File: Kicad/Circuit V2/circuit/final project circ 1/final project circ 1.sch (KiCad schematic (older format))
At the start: 87 parts, among them J1 USB_B_Micro, J10 Conn_01x02_Female, J11 Conn_01x02_Female, J12 Conn_01x02_Female, J2 Conn_01x01_Female, J3 Conn_01x04_Female, J4 Conn_01x04_Female, J5 Conn_01x03_Female, J6 Conn_01x03_Female, J7 Conn_01x04_Female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

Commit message: "finalized" the grounding stuff fixed more connections. Relay and Screw terminal still needs to be done. I should be able to finish it tonight
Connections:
- net +VDC: now also C12.1; no longer C12.2, U7.2 (Vin)
- net 12v: now also C10.1, C8.1, C9.1; no longer C10.2, C8.2, C9.2
- net GND1: now also C10.2, C11.2, C12.2, C13.2, C8.2, C9.2; no longer C10.1, C11.1, C12.1, C13.1, C8.1, C9.1
- net LINE: now also U7.2 (Vin)
- net at D3.1 (K), D4.1 (K), Q6.3 (C)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: now also C11.1; no longer C11.2
- net at D5.1 (K), Q6.1 (B), R8.1: now also C13.1; no longer C13.2
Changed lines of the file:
@@
 EESchema Schematic File Version 4
-EELAYER 30 0
+LIBS:final project circ 1-cache
+EELAYER 29 0
 EELAYER END
 $Descr A0 46811 33110
@@
 F 3 "~" H 18550 16550 50  0001 C CNN
 	1    18550 16550
-	-1   0    0    1
+	1    0    0    -1
 $EndComp
 $Comp
@@
 F 3 "~" H 19000 16550 50  0001 C CNN
 	1    19000 16550
-	-1   0    0    1
+	1    0    0    -1
 $EndComp
 Wire Wire Line
@@
 F 3 "~" H 19450 16550 50  0001 C CNN
 	1    19450 16550
-	-1   0    0    1
+	1    0    0    -1
 $EndComp
 Wire Wire Line
@@
 F 3 "~" H 15550 13800 50  0001 C CNN
 	1    15550 13800
-	-1   0    0    1
+	1    0    0    -1
 $EndComp
 Wire Wire Line
@@
 F 3 "~" H 16900 13900 50  0001 C CNN
 	1    16900 13900
-	-1   0    0    1
+	1    0    0    -1
 $EndComp
 Wire Wire Line
@@
 F 3 "~" H 16300 14450 50  0001 C CNN
 	1    16300 14450
-	-1   0    0    1
+	1    0    0    -1
 $EndComp
 Wire Wire Line
@@
 	1    0    0    -1
 $EndComp
-$Comp
-L power:+VDC #PWR036
-U 1 1 62176DF4
-P 19350 17950
-F 0 "#PWR036" H 19350 17850 50  0001 C CNN
-F 1 "+VDC" H 19350 18225 50  0000 C CNN
-F 2 "" H 19350 17950 50  0001 C CNN
-F 3 "" H 19350 17950 50  0001 C CNN
-	1    19350 17950
-	0    -1   -1   0
-$EndComp
-Wire Wire Line
-	19350 17950 19500 17950
 Wire Wire Line
 	19500 17950 19500 18000
@@
 Wire Wire Line
 	25700 10850 25700 10900
+$Comp
+L power:LINE #PWR0126
+U 1 1 6218464F
+P 19350 17950
+F 0 "#PWR0126" H 19350 17800 50  0001 C CNN
+F 1 "LINE" H 19367 18123 50  0000 C CNN
+F 2 "" H 19350 17950 50  0001 C CNN
+F 3 "" H 19350 17950 50  0001 C CNN
+	1    19350 17950
+	1    0    0    -1
+$EndComp
+Wire Wire Line
+	19350 17950 19500 17950
 $EndSCHEMATC

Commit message: one trace left baby!!
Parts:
- added C24: 100p, Capacitor_SMD:C_1210_3225Metric, symbol Device:C
- added OJ1, OJ2, OJ3, OJ4, OJ5, OJ6: SolderJumper_2_Open, Jumper:SolderJumper-2_P1.3mm_Open_Pad1.0x1.5mm, symbol Jumper:SolderJumper_2_Open
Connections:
- net GND: now also C24.1, OJ1.2 (B), OJ2.2 (B), OJ3.2 (B), OJ4.2 (B), OJ5.2 (B), OJ6.2 (B)
- net GND1: now also C24.2, OJ1.1 (A), OJ2.1 (A), OJ3.1 (A), OJ4.1 (A), OJ5.1 (A), OJ6.1 (A)
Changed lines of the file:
@@
 Wire Wire Line
 	19350 17950 19500 17950
+$Comp
+L final-project-circ-1-rescue:GND1-power #PWR?
+U 1 1 621A9CC9
+P 19300 21100
+F 0 "#PWR?" H 19300 20850 50  0001 C CNN
+F 1 "GND1" V 19305 20972 50  0000 R CNN
+F 2 "" H 19300 21100 50  0001 C CNN
+F 3 "" H 19300 21100 50  0001 C CNN
+	1    19300 21100
+	1    0    0    -1
+$EndComp
+$Comp
+L power:GND #PWR?
+U 1 1 621AB680
+P 19700 21100
+F 0 "#PWR?" H 19700 20850 50  0001 C CNN
+F 1 "GND" H 19705 20927 50  0000 C CNN
+F 2 "" H 19700 21100 50  0001 C CNN
+F 3 "" H 19700 21100 50  0001 C CNN
+	1    19700 21100
+	1    0    0    -1
+$EndComp
+$Comp
+L Device:C C24
+U 1 1 621ABDF7
+P 19500 21000
+F 0 "C24" V 19650 21000 50  0000 C CNN
+F 1 "100p" V 19339 21000 50  0000 C CNN
+F 2 "Capacitor_SMD:C_1210_3225Metric" H 19538 20850 50  0001 C CNN
+F 3 "~" H 19500 21000 50  0001 C CNN
+	1    19500 21000
+	0    1    1    0
+$EndComp
+Wire Wire Line
+	19350 21000 19300 21000
+Wire Wire Line
+	19300 21000 19300 21100
+Wire Wire Line
+	19650 21000 19700 21000
+Wire Wire Line
+	19700 21000 19700 21100
+$Comp
+L Jumper:SolderJumper_2_Open OJ1
+U 1 1 621F7E25
+P 19500 19200
+F 0 "OJ1" H 19500 19405 50  0000 C CNN
+F 1 "SolderJumper_2_Open" H 19500 19314 50  0000 C CNN
+F 2 "Jumper:SolderJumper-2_P1.3mm_Open_Pad1.0x1.5mm" H 19500 19200 50  0001 C CNN
+F 3 "~" H 19500 19200 50  0001 C CNN
+	1    19500 19200
+	1    0    0    -1
+$EndComp
+$Comp
+L Jumper:SolderJumper_2_Open OJ2
+U 1 1 62220007
+P 19500 19500
+F 0 "OJ2" H 19500 19705 50  0000 C CNN
+F 1 "SolderJumper_2_Open" H 19500 19614 50  0000 C CNN
+F 2 "Jumper:SolderJumper-2_P1.3mm_Open_Pad1.0x1.5mm" H 19500 19500 50  0001 C CNN
+F 3 "~" H 19500 19500 50  0001 C CNN
+	1    19500 19500
+	1    0    0    -1
+$EndComp
+$Comp
+L Jumper:SolderJumper_2_Open OJ3
+U 1 1 6222057A
+P 19500 19800
+F 0 "OJ3" H 19500 20005 50  0000 C CNN
+F 1 "SolderJumper_2_Open" H 19500 19914 50  0000 C CNN
+F 2 "Jumper:SolderJumper-2_P1.3mm_Open_Pad1.0x1.5mm" H 19500 19800 50  0001 C CNN
+F 3 "~" H 19500 19800 50  0001 C CNN
+	1    19500 19800
+	1    0    0    -1
+$EndComp
+$Comp
+L Jumper:SolderJumper_2_Open OJ4
+U 1 1 622208CB
+P 19500 20100
+F 0 "OJ4" H 19500 20305 50  0000 C CNN
+F 1 "SolderJumper_2_Open" H 19500 20214 50  0000 C CNN
+F 2 "Jumper:SolderJumper-2_P1.3mm_Open_Pad1.0x1.5mm" H 19500 20100 50  0001 C CNN
+F 3 "~" H 19500 20100 50  0001 C CNN
+	1    19500 20100
+	1    0    0    -1
+$EndComp
+$Comp
+L Jumper:SolderJumper_2_Open OJ5
+U 1 1 62247E3F
+P 19500 20400
+F 0 "OJ5" H 19500 20605 50  0000 C CNN
+F 1 "SolderJumper_2_Open" H 19500 20514 50  0000 C CNN
+F 2 "Jumper:SolderJumper-2_P1.3mm_Open_Pad1.0x1.5mm" H 19500 20400 50  0001 C CNN
+F 3 "~" H 19500 20400 50  0001 C CNN
+	1    19500 20400
+	1    0    0    -1
+$EndComp
+$Comp
+L Jumper:SolderJumper_2_Open OJ6
+U 1 1 622482E1
+P 19500 20700
+F 0 "OJ6" H 19500 20905 50  0000 C CNN
+F 1 "SolderJumper_2_Open" H 19500 20814 50  0000 C CNN
+F 2 "Jumper:SolderJumper-2_P1.3mm_Open_Pad1.0x1.5mm" H 19500 20700 50  0001 C CNN
+F 3 "~" H 19500 20700 50  0001 C CNN
+	1    19500 20700
+	1    0    0    -1
+$EndComp
+Wire Wire Line
+	19350 19200 19300 19200
+Wire Wire Line
+	19300 19200 19300 19500
+Connection ~ 19300 21000
+Wire Wire Line
+	19650 19200 19700 19200
+Wire Wire Line
+	19700 19200 19700 19500
+Connection ~ 19700 21000
+Wire Wire Line
+	19650 19500 19700 19500
+Connection ~ 19700 19500
+Wire Wire Line
+	19700 19500 19700 19800
+Wire Wire Line
+	19350 19500 19300 19500
+Connection ~ 19300 19500
+Wire Wire Line
+	19300 19500 19300 19800
+Wire Wire Line
+	19650 19800 19700 19800
+Connection ~ 19700 19800
+Wire Wire Line
+	19700 19800 19700 20100
+Wire Wire Line
+	19350 19800 19300 19800
+Connection ~ 19300 19800
+Wire Wire Line
+	19300 19800 19300 20100
+Wire Wire Line
+	19350 20100 19300 20100
+Connection ~ 19300 20100
+Wire Wire Line
+	19300 20100 19300 20400
+Wire Wire Line
+	19650 20100 19700 20100
+Connection ~ 19700 20100
+Wire Wire Line
+	19700 20100 19700 20400
+Wire Wire Line
+	19650 20400 19700 20400
+Connection ~ 19700 20400
+Wire Wire Line
+	19700 20400 19700 20700
+Wire Wire Line
+	19350 20400 19300 20400
+Connection ~ 19300 20400
+Wire Wire Line
+	19300 20400 19300 20700
+Wire Wire Line
+	19350 20700 19300 20700
+Connection ~ 19300 20700
+Wire Wire Line
+	19300 20700 19300 21000
+Wire Wire Line
+	19650 20700 19700 20700
+Connection ~ 19700 20700
+Wire Wire Line
+	19700 20700 19700 21000
 $EndSCHEMATC

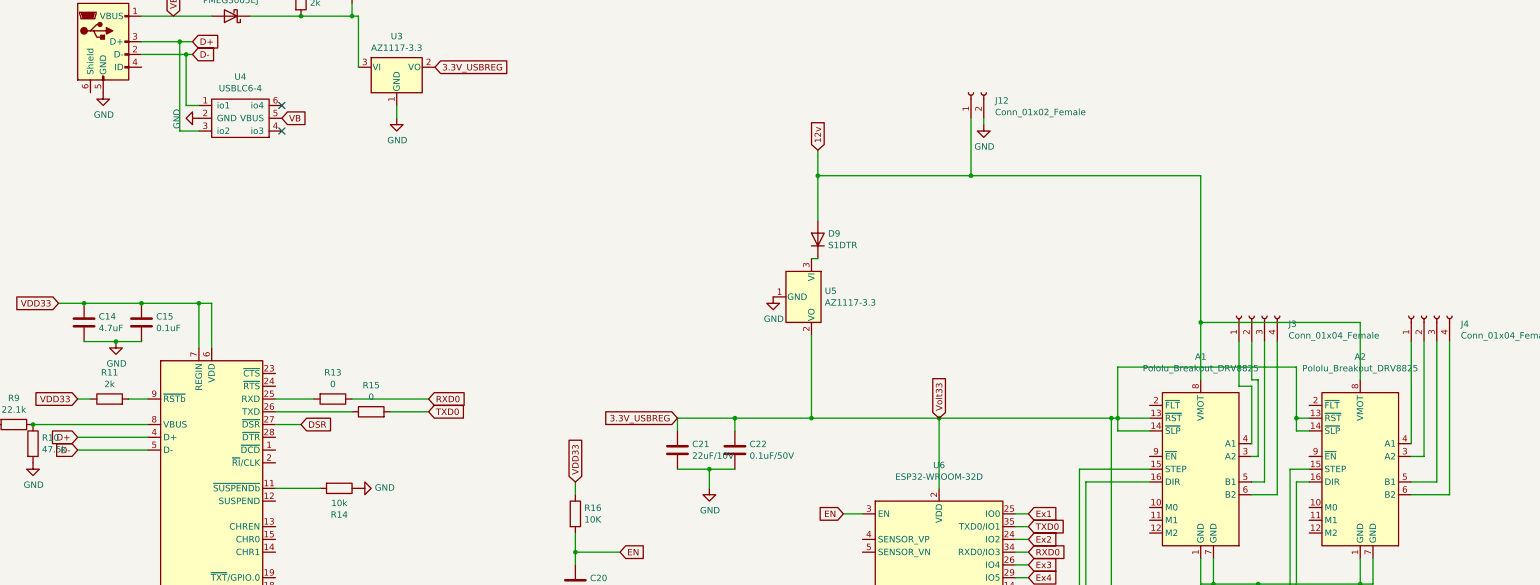
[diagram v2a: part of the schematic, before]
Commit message: changed stepper driver pinout
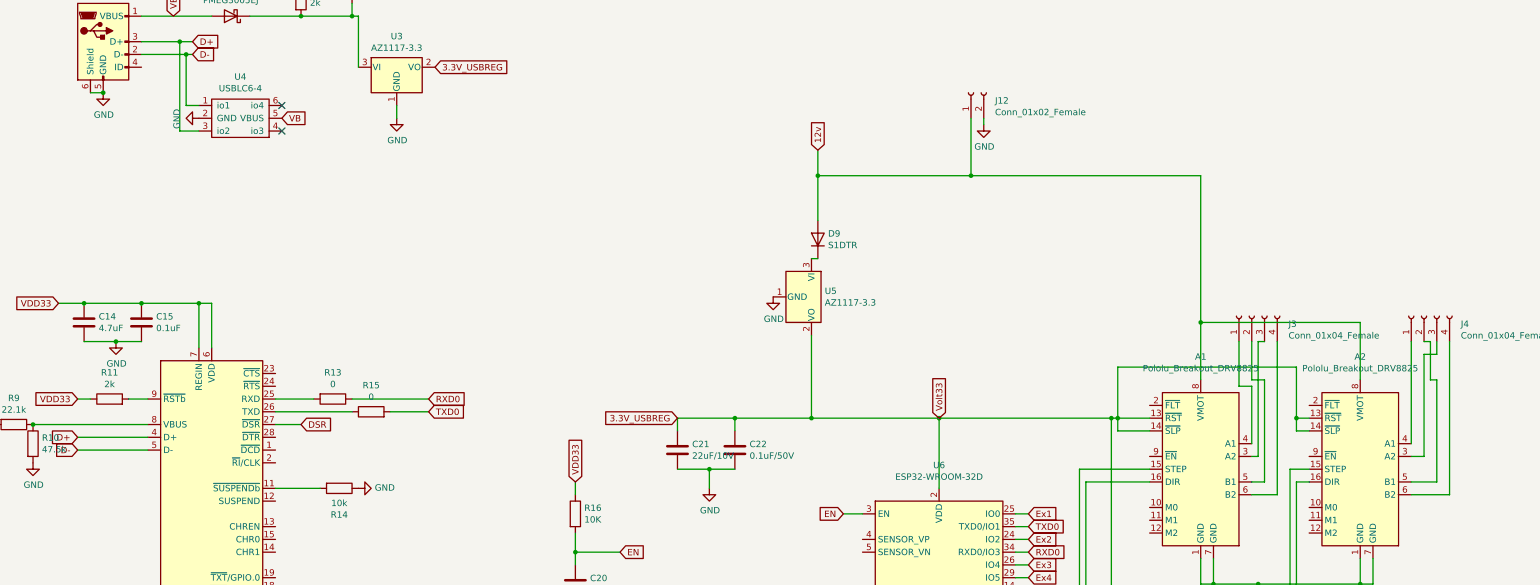
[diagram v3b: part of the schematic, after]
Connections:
- net GND: now also J1.6 (Shield)
- net at A1.3 (A2): now also J3.3 (Pin_3); no longer J3.2 (Pin_2)
- net at A1.5 (B1): now also J3.2 (Pin_2); no longer J3.3 (Pin_3)
- net at A2.3 (A2): now also J4.3 (Pin_3); no longer J4.2 (Pin_2)
- net at A2.5 (B1): now also J4.2 (Pin_2); no longer J4.3 (Pin_3)
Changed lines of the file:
@@
 EESchema Schematic File Version 4
-LIBS:final project circ 1-cache
-EELAYER 29 0
+EELAYER 30 0
 EELAYER END
 $Descr A0 46811 33110
@@
 $EndComp
 Wire Wire Line
-	27800 13400 27800 12950
-Wire Wire Line
 	27800 12950 27700 12950
 Wire Wire Line
@@
 	27800 12600 27800 12900
 Wire Wire Line
-	27800 12900 27850 12900
-Wire Wire Line
-	27850 12900 27850 13500
-Wire Wire Line
 	27850 13500 27800 13500
 Wire Wire Line
-	27900 12600 27900 13700
-Wire Wire Line
 	27900 13700 27800 13700
 Wire Wire Line
-	28000 12600 28000 13800
-Wire Wire Line
 	28000 13800 27800 13800
 Wire Wire Line
-	29050 12600 29050 13400
-Wire Wire Line
-	29150 12600 29150 13500
-Wire Wire Line
 	29150 13500 29050 13500
 Wire Wire Line
-	29250 12600 29250 13700
-Wire Wire Line
 	29250 13700 29050 13700
-Wire Wire Line
-	29350 12600 29350 13800
 Wire Wire Line
 	29350 13800 29050 13800
@@
 	19350 17950 19500 17950
 $Comp
-L final-project-circ-1-rescue:GND1-power #PWR?
+L final-project-circ-1-rescue:GND1-power #PWR0127
 U 1 1 621A9CC9
 P 19300 21100
-F 0 "#PWR?" H 19300 20850 50  0001 C CNN
+F 0 "#PWR0127" H 19300 20850 50  0001 C CNN
 F 1 "GND1" V 19305 20972 50  0000 R CNN
 F 2 "" H 19300 21100 50  0001 C CNN
@@
 $EndComp
 $Comp
-L power:GND #PWR?
+L power:GND #PWR0128
 U 1 1 621AB680
 P 19700 21100
-F 0 "#PWR?" H 19700 20850 50  0001 C CNN
+F 0 "#PWR0128" H 19700 20850 50  0001 C CNN
 F 1 "GND" H 19705 20927 50  0000 C CNN
 F 2 "" H 19700 21100 50  0001 C CNN
@@
 Wire Wire Line
 	19700 20700 19700 21000
+Wire Wire Line
+	18700 10650 18800 10650
+Connection ~ 18800 10650
+Wire Wire Line
+	27800 12950 27800 13400
+Wire Wire Line
+	27900 13700 27900 12900
+Wire Wire Line
+	27800 12900 27900 12900
+Wire Wire Line
+	27850 13500 27850 12600
+Wire Wire Line
+	27850 12600 27900 12600
+Wire Wire Line
+	28000 13800 28000 12600
+Wire Wire Line
+	29050 13400 29050 12600
+Wire Wire Line
+	29250 12900 29200 12900
+Wire Wire Line
+	29200 12900 29200 12600
+Wire Wire Line
+	29200 12600 29150 12600
+Wire Wire Line
+	29250 12900 29250 13700
+Wire Wire Line
+	29150 13500 29150 12700
+Wire Wire Line
+	29150 12700 29250 12700
+Wire Wire Line
+	29250 12700 29250 12600
+Wire Wire Line
+	29350 13800 29350 12600
 $EndSCHEMATC

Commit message: actually finished test PCB
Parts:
- removed J2: Conn_01x01_Female, symbol Connector:Conn_01x01_Female
- added J13: Conn_01x03, Connector_PinHeader_2.54mm:PinHeader_1x03_P2.54mm_Vertical, symbol Connector_Generic:Conn_01x03
- added J2: Conn_01x06, SDESIGN:new_screw_term, symbol Connector_Generic:Conn_01x06
- J5, J6: footprint bigboard:encoder_out -> bigboard:PEC12R-4117F-N0012
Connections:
- net 12v: now also J13.1 (Pin_1)
- net Ex2: now also J13.2 (Pin_2)
- net GND: now also J13.3 (Pin_3), J2.5 (Pin_5), J2.6 (Pin_6)
- net LINE: now also J2.1 (Pin_1)
- net NEUT: now also J2.2 (Pin_2), J2.3 (Pin_3)
- net at A1.3 (A2): now also J3.1 (Pin_1); no longer J3.3 (Pin_3)
- net at A1.4 (A1): now also J3.2 (Pin_2); no longer J3.1 (Pin_1)
- net at A1.5 (B1): now also J3.3 (Pin_3); no longer J3.2 (Pin_2)
- net at A2.3 (A2): now also J4.1 (Pin_1); no longer J4.3 (Pin_3)
- net at A2.4 (A1): now also J4.2 (Pin_2); no longer J4.1 (Pin_1)
- net at A2.5 (B1): now also J4.3 (Pin_3); no longer J4.2 (Pin_2)
- net LineOut: now reaches U7.5 (Output)
- net LineOut: now also J2.4 (Pin_4)
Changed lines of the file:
@@
 EESchema Schematic File Version 4
-EELAYER 30 0
+LIBS:final project circ 1-cache
+EELAYER 29 0
 EELAYER END
 $Descr A0 46811 33110
@@
 	0    -1   -1   0
 $EndComp
-Wire Wire Line
-	27800 12950 27700 12950
-Wire Wire Line
-	27700 12950 27700 12600
-Wire Wire Line
-	27800 12600 27800 12900
-Wire Wire Line
-	27850 13500 27800 13500
-Wire Wire Line
-	27900 13700 27800 13700
-Wire Wire Line
-	28000 13800 27800 13800
-Wire Wire Line
-	29150 13500 29050 13500
-Wire Wire Line
-	29250 13700 29050 13700
-Wire Wire Line
-	29350 13800 29050 13800
 Wire Wire Line
 	27000 13200 26750 13200
@@
 F 0 "J5" H 29978 15176 50  0000 L CNN
 F 1 "Conn_01x03_Female" H 29978 15085 50  0000 L CNN
-F 2 "bigboard:encoder_out" H 29950 15150 50  0001 C CNN
+F 2 "bigboard:PEC12R-4117F-N0012" H 29950 15150 50  0001 C CNN
 F 3 "~" H 29950 15150 50  0001 C CNN
 	1    29950 15150
@@
 F 0 "J6" V 29938 16612 50  0000 R CNN
 F 1 "Conn_01x03_Female" V 29847 16612 50  0000 R CNN
-F 2 "bigboard:encoder_out" H 30000 16800 50  0001 C CNN
+F 2 "bigboard:PEC12R-4117F-N0012" H 30000 16800 50  0001 C CNN
 F 3 "~" H 30000 16800 50  0001 C CNN
 	1    30000 16800
@@
 Text GLabel 20100 18000 2    50   Input ~ 0
 EX1
-$Comp
-L Connector:Conn_01x01_Female J2
-U 1 1 622786E8
-P 20300 18100
-F 0 "J2" H 20328 18126 50  0000 L CNN
-F 1 "Conn_01x01_Female" H 20328 18035 50  0000 L CNN
-F 2 "" H 20300 18100 50  0001 C CNN
-F 3 "~" H 20300 18100 50  0001 C CNN
-	1    20300 18100
-	1    0    0    -1
-$EndComp
 Wire Wire Line
 	21850 18350 21850 19250
@@
 Connection ~ 18800 10650
 Wire Wire Line
-	27800 12950 27800 13400
-Wire Wire Line
-	27900 13700 27900 12900
-Wire Wire Line
-	27800 12900 27900 12900
-Wire Wire Line
-	27850 13500 27850 12600
-Wire Wire Line
-	27850 12600 27900 12600
+	27800 13500 27900 13500
+Wire Wire Line
+	27900 13500 27900 12850
+Wire Wire Line
+	27900 12850 27700 12850
+Wire Wire Line
+	27700 12850 27700 12600
+Wire Wire Line
+	27800 13400 27800 12600
+Wire Wire Line
+	27800 13700 27950 13700
+Wire Wire Line
+	27950 13700 27950 12750
+Wire Wire Line
+	27950 12750 27900 12750
+Wire Wire Line
+	27900 12750 27900 12600
+Wire Wire Line
+	27800 13800 28000 13800
 Wire Wire Line
 	28000 13800 28000 12600
-Wire Wire Line
-	29050 13400 29050 12600
-Wire Wire Line
-	29250 12900 29200 12900
-Wire Wire Line
-	29200 12900 29200 12600
-Wire Wire Line
-	29200 12600 29150 12600
-Wire Wire Line
-	29250 12900 29250 13700
-Wire Wire Line
-	29150 13500 29150 12700
-Wire Wire Line
-	29150 12700 29250 12700
-Wire Wire Line
-	29250 12700 29250 12600
+$Comp
+L Connector_Generic:Conn_01x06 J2
+U 1 1 62274E2D
+P 13600 13500
+F 0 "J2" H 13680 13492 50  0000 L CNN
+F 1 "Conn_01x06" H 13680 13401 50  0000 L CNN
+F 2 "SDESIGN:new_screw_term" H 13600 13500 50  0001 C CNN
+F 3 "~" H 13600 13500 50  0001 C CNN
+	1    13600 13500
+	1    0    0    -1
+$EndComp
+$Comp
+L power:LINE #PWR0129
+U 1 1 622781AF
+P 13400 13300
+F 0 "#PWR0129" H 13400 13150 50  0001 C CNN
+F 1 "LINE" H 13417 13473 50  0000 C CNN
+F 2 "" H 13400 13300 50  0001 C CNN
+F 3 "" H 13400 13300 50  0001 C CNN
+	1    13400 13300
+	0    -1   -1   0
+$EndComp
+$Comp
+L power:NEUT #PWR0130
+U 1 1 62278FA3
+P 13400 13400
+F 0 "#PWR0130" H 13400 13250 50  0001 C CNN
+F 1 "NEUT" H 13417 13573 50  0000 C CNN
+F 2 "" H 13400 13400 50  0001 C CNN
+F 3 "" H 13400 13400 50  0001 C CNN
+	1    13400 13400
+	0    -1   -1   0
+$EndComp
+$Comp
+L power:NEUT #PWR0131
+U 1 1 62279B38
+P 13400 13500
+F 0 "#PWR0131" H 13400 13350 50  0001 C CNN
+F 1 "NEUT" H 13417 13673 50  0000 C CNN
+F 2 "" H 13400 13500 50  0001 C CNN
+F 3 "" H 13400 13500 50  0001 C CNN
+	1    13400 13500
+	0    -1   -1   0
+$EndComp
+Text GLabel 20100 18100 2    50   Input ~ 0
+LineOut
+Text GLabel 13400 13600 0    50   Input ~ 0
+LineOut
+$Comp
+L power:GND #PWR0132
+U 1 1 6227AC04
+P 13400 13700
+F 0 "#PWR0132" H 13400 13450 50  0001 C CNN
+F 1 "GND" H 13405 13527 50  0000 C CNN
+F 2 "" H 13400 13700 50  0001 C CNN
+F 3 "" H 13400 13700 50  0001 C CNN
+	1    13400 13700
+	0    1    1    0
+$EndComp
+$Comp
+L power:GND #PWR0133
+U 1 1 6227B6B1
+P 13400 13800
+F 0 "#PWR0133" H 13400 13550 50  0001 C CNN
+F 1 "GND" H 13405 13627 50  0000 C CNN
+F 2 "" H 13400 13800 50  0001 C CNN
+F 3 "" H 13400 13800 50  0001 C CNN
+	1    13400 13800
+	0    1    1    0
+$EndComp
+Wire Wire Line
+	29100 13500 29050 13500
+Wire Wire Line
+	29100 13500 29100 12850
+Wire Wire Line
+	29100 12850 29050 12850
+Wire Wire Line
+	29050 12850 29050 12600
+Wire Wire Line
+	29050 13400 29150 13400
+Wire Wire Line
+	29150 13400 29150 12600
+Wire Wire Line
+	29050 13700 29250 13700
+Wire Wire Line
+	29250 13700 29250 12600
+Wire Wire Line
+	29050 13800 29350 13800
 Wire Wire Line
 	29350 13800 29350 12600
+$Comp
+L Connector_Generic:Conn_01x03 J13
+U 1 1 622AE256
+P 22450 11800
+F 0 "J13" H 22530 11842 50  0000 L CNN
+F 1 "Conn_01x03" H 22530 11751 50  0000 L CNN
+F 2 "Connector_PinHeader_2.54mm:PinHeader_1x03_P2.54mm_Vertical" H 22450 11800 50  0001 C CNN
+F 3 "~" H 22450 11800 50  0001 C CNN
+	1    22450 11800
+	1    0    0    -1
+$EndComp
+Text GLabel 22250 11700 0    50   Input ~ 0
+12v
+Text GLabel 22250 11800 0    50   Input ~ 0
+Ex2
+$Comp
+L power:GND #PWR01
+U 1 1 622AF5A3
+P 22250 11900
+F 0 "#PWR01" H 22250 11650 50  0001 C CNN
+F 1 "GND" H 22255 11727 50  0000 C CNN
+F 2 "" H 22250 11900 50  0001 C CNN
+F 3 "" H 22250 11900 50  0001 C CNN
+	1    22250 11900
+	1    0    0    -1
+$EndComp
 $EndSCHEMATC
